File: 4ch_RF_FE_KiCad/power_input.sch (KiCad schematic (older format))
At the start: 8 parts

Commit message: initial completion of schematic capture
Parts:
- removed C? (x2): 1000pF, symbol Device:C
- removed C?: 1uF, symbol Device:C
- removed J?: PJ1-021-SMT-TR, CUI_PJ1-021-SMT-TR, symbol PJ1-021-SMT-TR:PJ1-021-SMT-TR
- removed L?: ACP3225, symbol jcg_custom_parts:ACP3225
- added C1, C12, C26, C4: 0.1µF, Capacitor_SMD:C_0402_1005Metric, symbol Device:C
- added C10, C11, C13, C14, C15, C16, C17, C18, C19, C20, C21, C22, C23, C24, C25, C7, C8, C9: 10µF, Capacitor_SMD:C_1206_3216Metric_Pad1.42x1.75mm_HandSolder, symbol Device:C
- added C27: 22µF, Capacitor_SMD:C_1206_3216Metric_Pad1.42x1.75mm_HandSolder, symbol Device:C
- added C3, C5, C6: 1µF, Capacitor_SMD:C_0603_1608Metric_Pad1.05x0.95mm_HandSolder, symbol Device:C
- added DS1: LTST-C190KGKT, digikey-footprints:LED_0603, symbol dk_LED-Indication-Discrete:LTST-C190KGKT
- added J1: PJ1-021-SMT-TR, footprints:CUI_PJ1-021-SMT-TR, symbol PJ1-021-SMT-TR:PJ1-021-SMT-TR
- added L1: ACP3225, jcg_custom:CMC_3225_2x2_LGA, symbol jcg_custom_parts:ACP3225
- added L2: SRR6038-3R3Y, footprints:SRR6038-3R3Y, symbol SRR6038-3R3Y:SRR6038-3R3Y
- added R2, R3: 10, Resistor_SMD:R_0402_1005Metric, symbol Device:R_US
- added R4: 100k, Resistor_SMD:R_0402_1005Metric, symbol Device:R_US
- added R5: CSR1206-0R002F1, jcg_custom:CSR_4pin_1206_3216Metric_Pad1.42x1.75mm_HandSolder, symbol jcg_custom_parts:CSR1206-0R002F1
- added R6: 180, Resistor_SMD:R_0603_1608Metric_Pad1.05x0.95mm_HandSolder, symbol Device:R_US
- added R7: 61.9k, Resistor_SMD:R_0402_1005Metric, symbol Device:R_US
- added R8: 10k, Resistor_SMD:R_0402_1005Metric, symbol Device:R_US
- added U1, U2, U3, U4: MCP1755ST-5002E_DB, footprints:MCP1755ST-5002E_DB, symbol MCP1755ST-5002E_DB:MCP1755ST-5002E_DB
- added U5: INA219AIDCNR, digikey-footprints:SOT-23-8, symbol dk_PMIC-Current-Regulation-Management:INA219AIDCNR
- added U6: TPS562208DDCT, footprints:TPS562208DDCT, symbol TPS562208DDCT:TPS562208DDCT
- C2: renamed from C?; value C0402 DNP -> DNP; footprint (none) -> Capacitor_SMD:C_0402_1005Metric
- R1: renamed from R?; value R0402 DNP -> DNP; footprint (none) -> Resistor_SMD:R_0402_1005Metric
- gave numbers to parts that had none: 1
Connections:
- net GND: now also C1.2, C10.2, C11.2, C12.2, C13.2, C14.2, C15.2, C16.2, C17.2, C18.2, C19.2, C20.2, C21.2, C22.2, C23.2, C24.2, C25.2, C27.2, C5.2, C7.2, C8.2, C9.2, L1.3, R4.2, R6.2, R8.2, U1.2 (GND), U2.2 (GND), U3.2 (GND), U4.2 (GND), U5.3 (GND), U5.7 (A0), U5.8 (A1), U6.1 (GND)
- net at F1.1: now also J1.1
- net at C2.2, R1.2: now also C1.1, C3.2, C4.1, J1.2, J1.3, L1.2
- net at F1.2: now also C3.1, C4.2, L1.1
- new net: C11.1, C5.1, L1.4, R4.1, R5.1
- new net: C6.1, R2.1, U5.1 (IN+)
- new net: C6.2, R3.1, U5.2 (IN-)
- new net: C26.1, U6.6 (VBST)
- new net: C26.2, L2.2, U6.2 (SW)
- new net: R7.2, R8.1, U6.4 (VFB)
- new net: DS1.1, R6.1
- new net +3V3: C12.1, U5.4 (VS)
- new net +5V_CH0: C13.1, C17.1, C21.1, U1.3 (VOUT)
- new net +5V_CH1: C14.1, C18.1, C22.1, U2.3 (VOUT)
- new net +5V_CH2: C15.1, C19.1, C23.1, U3.3 (VOUT)
- new net +5V_CH3: C16.1, C20.1, C24.1, U4.3 (VOUT)
- new net 5V5_SW: C10.1, C27.1, C7.1, C8.1, C9.1, DS1.2, L2.1, R7.1, U1.1 (VIN), U2.1 (VIN), U3.1 (VIN), U4.1 (VIN)
- new net INA_I2C_SCL: U5.5 (SCL)
- new net INA_I2C_SDA: U5.6 (SDA)
- new net Vin_unreg: C25.1, R5.3, U6.3 (VIN), U6.5 (EN)
- new net sense12V_N: R3.2, R5.2
- new net sense12V_P: R2.2, R5.4
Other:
- note added: "3.3 uH 20 mOhm DCR\n3.5A Rated"
- note added: "5.5V -> 5V, Per Channel LDO"
- note added: "9V-12V Input -> 5.5V SMPS Regulated"
- note added: "Addr: 0x40"
- note added: "DC Power Input"
- note added: "Iout_max = 250 mA (per RF Channel)\nP_LDO_max => (Vin - Vout)*Iout_max = 125 mW\nR_JA = 62.0 degC/W (typ, SOT-223-3)\nTJ_rise_max => P_LDO_max*R_JA = 7.75 degC\n\nPSRR = 80 dB\nLine Regulation = +/- 0.01% (typ)"
- note added: "PWR Good LED\nVf: 1.9V - 2.4V\nIF: 20 mA"
- note added: "Per LDO:"
- note added: "Vout: 5.5 V\nVripple: 39.5 mV (pk-pk)\nIout : 2 A (max)\nEfficiency: 93% (typ)"
- note removed: "Typ: 12V\n ?A\nMax: ?V\n 2A"
- moved on the sheet: C2, F1, R1

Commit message: (+) starting layout
Signed-off-by: Gentile, John <johncgentile17@gmail.com>
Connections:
- net sense12V_N: now also R5.4; no longer R5.2
- net sense12V_P: now also R5.2; no longer R5.4
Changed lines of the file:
@@
 Wire Wire Line
 	6800 1700 6850 1700
+Text Label 6850 1800 0    50   ~ 0
+sense12V_P
 Text Label 6850 1700 0    50   ~ 0
-sense12V_P
-Text Label 6850 1800 0    50   ~ 0
 sense12V_N
 Wire Wire Line

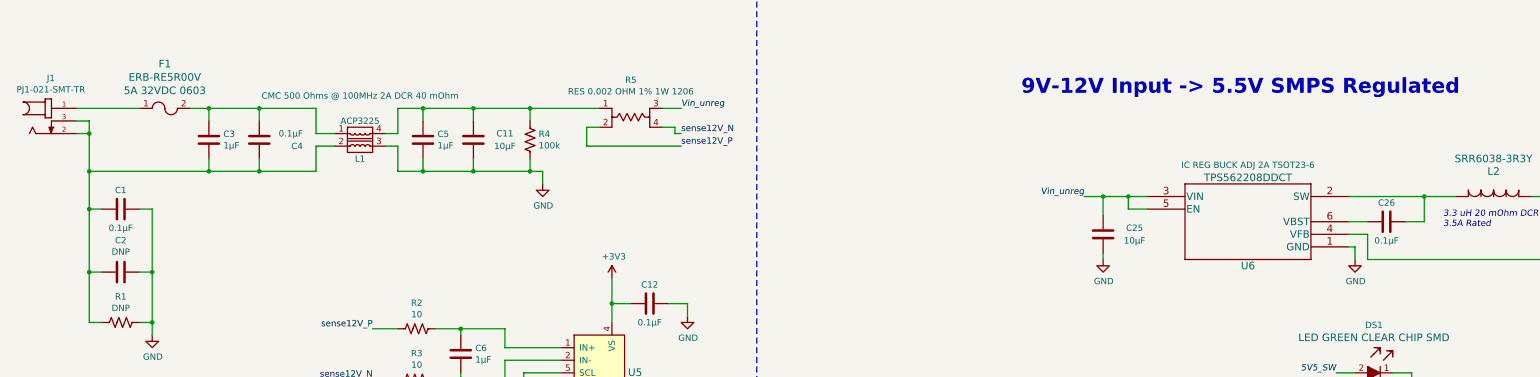
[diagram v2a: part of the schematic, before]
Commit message: (+) power & DIO layout & impedance calcs
Signed-off-by: Gentile, John <johncgentile17@gmail.com>
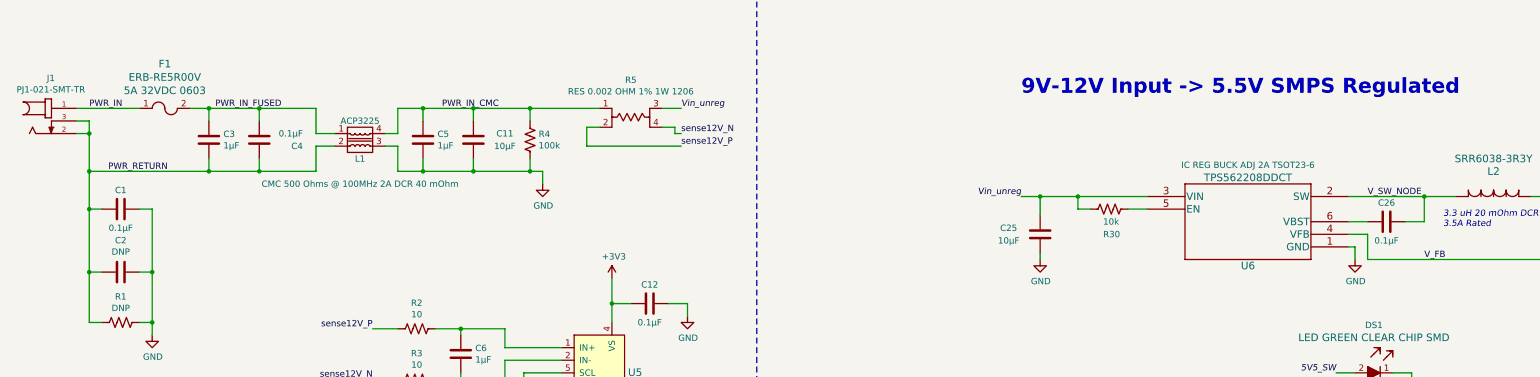
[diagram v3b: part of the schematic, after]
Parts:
- added R30: 10k, Resistor_SMD:R_0402_1005Metric, symbol Device:R_US
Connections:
- net Vin_unreg: now also R30.2; no longer U6.5 (EN)
- net PWR_RETURN: now reaches C1.1, C2.2, C3.2, C4.1, J1.2, J1.3, L1.2, R1.2
- net PWR_IN: now reaches F1.1, J1.1
- net PWR_IN_FUSED: now reaches C3.1, C4.2, F1.2, L1.1
- net PWR_IN_CMC: now reaches C11.1, C5.1, L1.4, R4.1, R5.1
- net V_SW_NODE: now reaches C26.2, L2.2, U6.2 (SW)
- net V_FB: now reaches R7.2, R8.1, U6.4 (VFB)
- new net: R30.1, U6.5 (EN)
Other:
- moved on the sheet: C25
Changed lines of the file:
@@
 $EndComp
 Wire Wire Line
-	10550 2200 10400 2200
-Wire Wire Line
-	10400 2200 10400 2300
-Wire Wire Line
-	10400 2300 10550 2300
-Wire Wire Line
-	10200 2350 10200 2200
-Wire Wire Line
-	10200 2200 10400 2200
-Connection ~ 10400 2200
+	9700 2350 9700 2200
 $Comp
 L power:GND #PWR014
 U 1 1 5F8C519E
-P 10200 2700
-F 0 "#PWR014" H 10200 2450 50  0001 C CNN
-F 1 "GND" H 10205 2527 50  0000 C CNN
-F 2 "" H 10200 2700 50  0001 C CNN
-F 3 "" H 10200 2700 50  0001 C CNN
-	1    10200 2700
-	1    0    0    -1
-$EndComp
-Wire Wire Line
-	10200 2700 10200 2650
+P 9700 2700
+F 0 "#PWR014" H 9700 2450 50  0001 C CNN
+F 1 "GND" H 9705 2527 50  0000 C CNN
+F 2 "" H 9700 2700 50  0001 C CNN
+F 3 "" H 9700 2700 50  0001 C CNN
+	1    9700 2700
+	1    0    0    -1
+$EndComp
+Wire Wire Line
+	9700 2700 9700 2650
 Wire Wire Line
 	12150 2400 12300 2400
@@
 Wire Wire Line
 	6850 1500 6700 1500
-Text Label 10050 2200 2    50   Italic 0
+Text Label 9550 2200 2    50   Italic 0
 Vin_unreg
 Wire Wire Line
-	10050 2200 10200 2200
-Connection ~ 10200 2200
+	9550 2200 9700 2200
+Connection ~ 9700 2200
 Text Label 14500 2200 0    50   Italic 0
 5V5_SW
@@
 F 2 "jcg_custom:CMC_3225_2x2_LGA" H 4300 1500 50  0001 C CNN
 F 3 "https://product.tdk.com/info/en/catalog/datasheets/cmf_commercial_power_acp3225_en.pdf" H 4300 1800 50  0001 C CNN
-F 4 "CMC 500 Ohms @ 100MHz 2A DCR 40 mOhm" H 4300 2100 50  0000 C CNN "Description"
+F 4 "CMC 500 Ohms @ 100MHz 2A DCR 40 mOhm" H 4300 1400 50  0000 C CNN "Description"
 F 5 "445-172408-1-ND" H 4300 2250 50  0001 C CNN "Digi-Key PN"
 	1    4300 1750
@@
 L Device:C C?
 U 1 1 5E79CAAE
-P 10200 2500
+P 9700 2500
 AR Path="/5E79CAAE" Ref="C?"  Part="1"
 AR Path="/5E5AB76A/5E79CAAE" Ref="C?"  Part="1"
 AR Path="/5E86F12A/5E79CAAE" Ref="C?"  Part="1"
 AR Path="/5E5BBCD5/5E79CAAE" Ref="C25"  Part="1"
-F 0 "C25" H 9950 2550 50  0000 C CNN
-F 1 "10µF" H 9950 2450 50  0000 C CNN
-F 2 "Capacitor_SMD:C_1206_3216Metric_Pad1.42x1.75mm_HandSolder" V 10040 2500 50  0001 C CNN
-F 3 "http://www.samsungsem.com/kr/support/product-search/mlcc/CL31B106KAHNNNE.jsp" H 10200 2500 50  0001 C CNN
-F 4 "1276-1804-1-ND" H 10200 2500 50  0001 C CNN "Digi-Key PN"
-F 5 "10µF ±10% 25V Ceramic Capacitor X7R 1206 (3216 Metric)" H 10200 2500 50  0001 C CNN "Description"
-	1    10200 2500
-	-1   0    0    -1
+F 0 "C25" H 9450 2550 50  0000 C CNN
+F 1 "10µF" H 9450 2450 50  0000 C CNN
+F 2 "Capacitor_SMD:C_1206_3216Metric_Pad1.42x1.75mm_HandSolder" V 9540 2500 50  0001 C CNN
+F 3 "http://www.samsungsem.com/kr/support/product-search/mlcc/CL31B106KAHNNNE.jsp" H 9700 2500 50  0001 C CNN
+F 4 "1276-1804-1-ND" H 9700 2500 50  0001 C CNN "Digi-Key PN"
+F 5 "10µF ±10% 25V Ceramic Capacitor X7R 1206 (3216 Metric)" H 9700 2500 50  0001 C CNN "Description"
+	1    9700 2500
+	1    0    0    -1
 $EndComp
 $Comp
@@
 	-1   0    0    -1
 $EndComp
+Text Label 2150 1500 0    50   ~ 0
+PWR_IN
+Text Label 3150 1500 0    50   ~ 0
+PWR_IN_FUSED
+Text Label 4950 1500 0    50   ~ 0
+PWR_IN_CMC
+Text Label 2300 2000 0    50   ~ 0
+PWR_RETURN
+Text Label 12300 2200 0    50   ~ 0
+V_SW_NODE
+Text Label 12750 2700 0    50   ~ 0
+V_FB
+$Comp
+L Device:R_US R?
+U 1 1 5E70F1EB
+P 10250 2300
+AR Path="/5E86F12A/5E70F1EB" Ref="R?"  Part="1"
+AR Path="/5E5BBCD5/5E70F1EB" Ref="R30"  Part="1"
+F 0 "R30" V 10450 2250 50  0000 L CNN
+F 1 "10k" V 10350 2250 50  0000 L CNN
+F 2 "Resistor_SMD:R_0402_1005Metric" V 10290 2290 50  0001 C CNN
+F 3 "https://www.yageo.com/upload/media/product/productsearch/datasheet/rchip/PYu-RC_Group_51_RoHS_L_10.pdf" H 10250 2300 50  0001 C CNN
+F 4 "311-10.0KLRCT-ND" H 10250 2300 50  0001 C CNN "Digi-Key PN"
+F 5 "10 kOhms ±1% 0.063W, 1/16W Chip Resistor 0402 (1005 Metric) Moisture Resistant Thick Film" H 10250 2300 50  0001 C CNN "Description"
+	1    10250 2300
+	0    1    1    0
+$EndComp
+Wire Wire Line
+	10100 2300 10000 2300
+Wire Wire Line
+	10000 2300 10000 2200
+Wire Wire Line
+	9700 2200 10000 2200
+Wire Wire Line
+	10000 2200 10550 2200
+Connection ~ 10000 2200
+Wire Wire Line
+	10400 2300 10550 2300
 $EndSCHEMATC
